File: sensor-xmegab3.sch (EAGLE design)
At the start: 59 parts, among them IC3 ATmega169PA, K1 SP6029TOP, M1 NRF24L01P-M, M2 DHT22, Q1 IRLML2502, Q2 IRLML2502, Q3 IRLML6402, U1 MCP1640C, U2 MCP604-I/ST

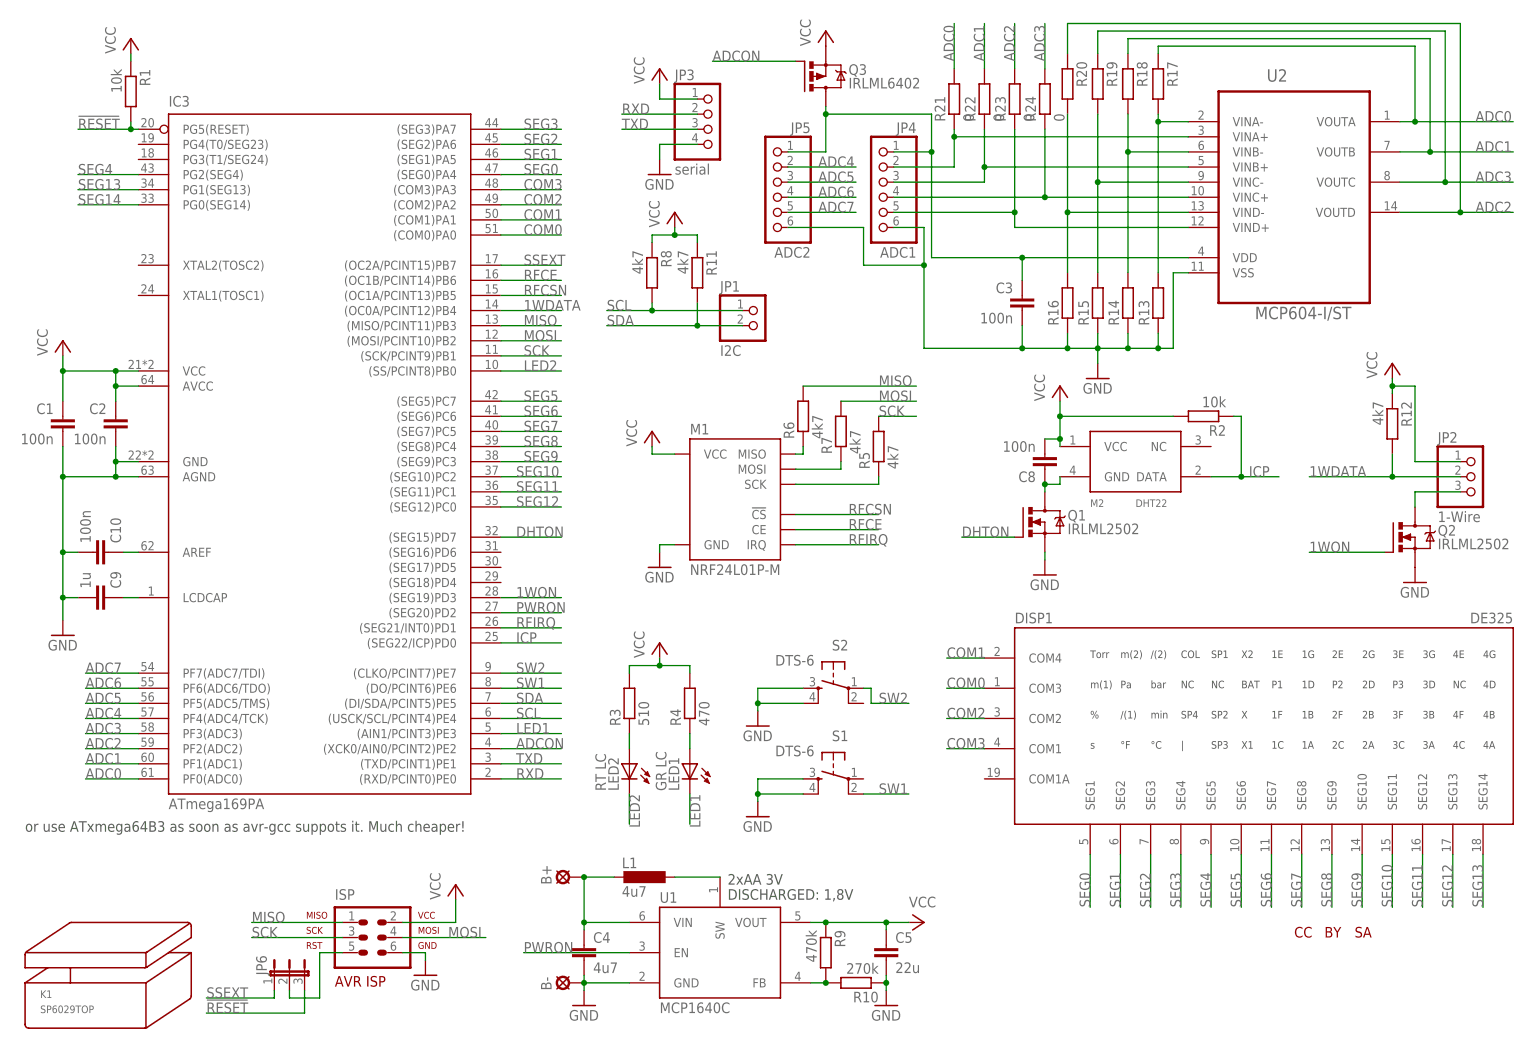
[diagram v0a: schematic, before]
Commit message: hanged to xmega, better performance at lower price
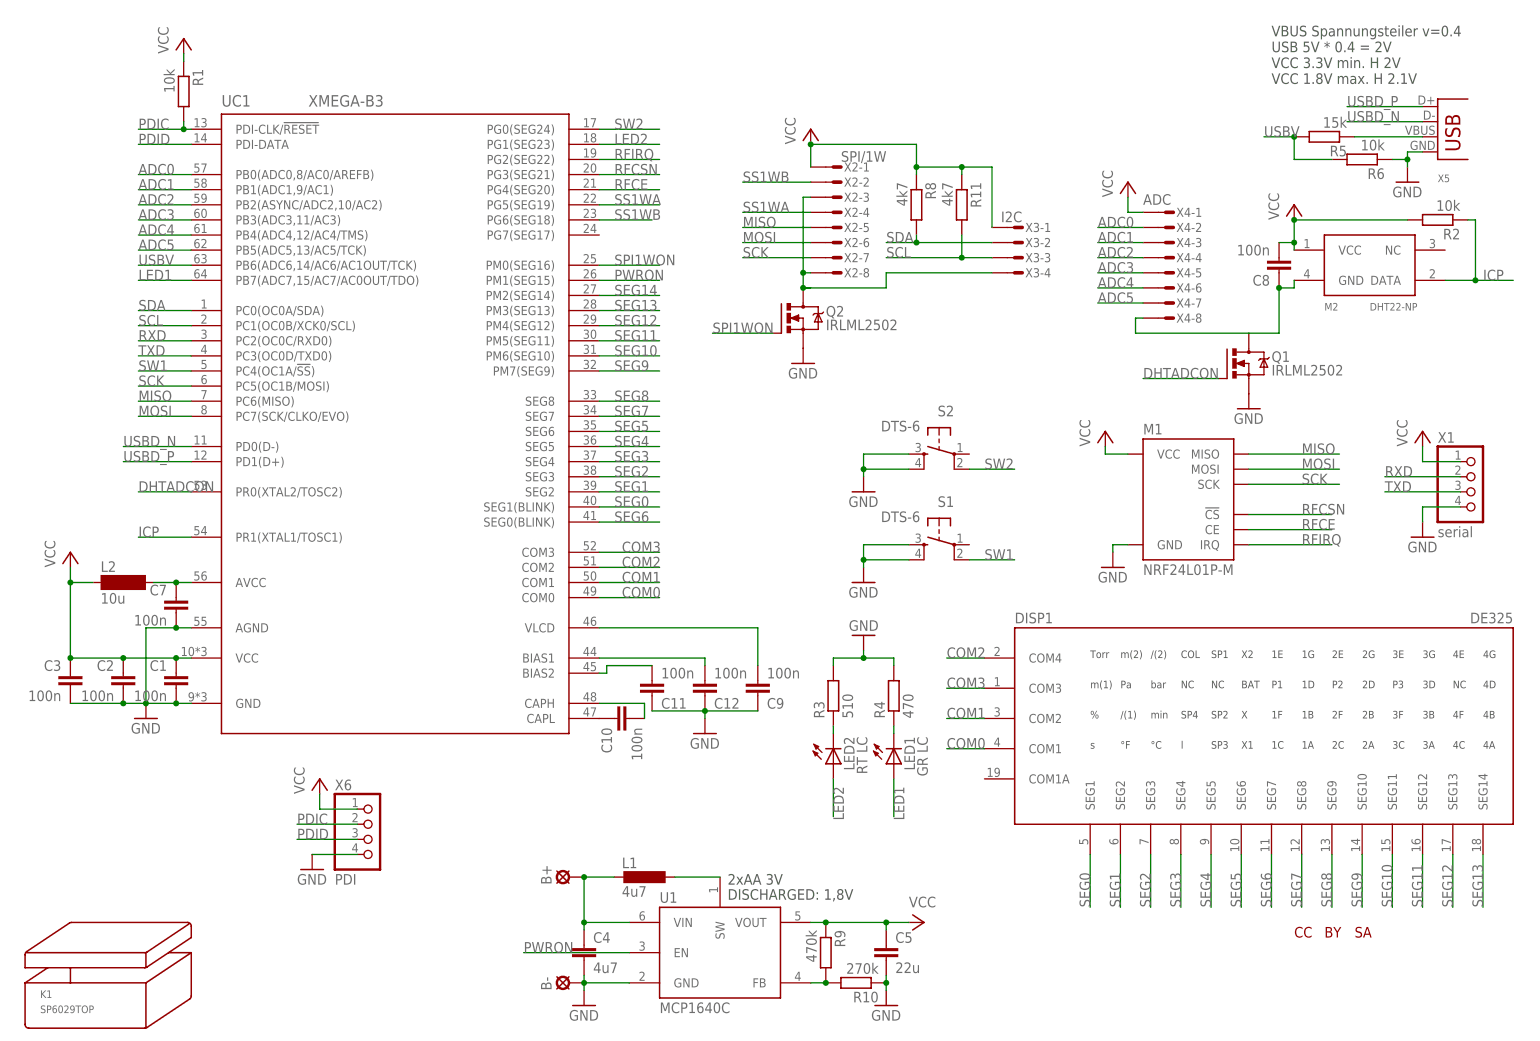
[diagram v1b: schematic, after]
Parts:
- removed IC3: ATmega169PA, avr-7:MEGA169-A
- removed ISP: ML6, avr-7:AVR-ISP-6VERT
- removed JP1: I2C, pinhead-mod:PINHD-1X2_2.54
- removed JP2: 1-Wire, pinhead-mod:PINHD-1X3_2.54
- removed JP3: serial, pinhead-mod:PINHD-1X4_2.54
- removed JP4: ADC1, pinhead-mod:PINHD-1X6_2.54
- removed JP5: ADC2, pinhead-mod:PINHD-1X6_2.54
- removed JP6: (no value), jumper:JP2E
- removed Q3: IRLML6402, mosfet:IRLML6402
- removed R12, R7: 4k7, rcl:R-EU_R0603
- removed R13, R14, R15, R16, R17, R18, R19, R20: (no value), rcl:R-EU_R0603
- removed R21, R22, R23, R24: 0, rcl:R-EU_R0201
- removed U2: MCP604-I/ST, microchip:MCP604-I/ST
- added C11, C12, C7: 100n, rcl:C-EUC0603
- added L2: 10u, inductor-neosid:SM-NE29
- added UC1: XMEGA-B3, avr-7:XMEGA-B3
- added X1: serial, pinhead-mod:PINHD-1X4_2.54
- added X2: SPI/1W, con-amp-micromatch:MICROMATCH-8
- added X3: I2C, con-amp-micromatch:MICROMATCH-4
- added X4: ADC, con-amp-micromatch:MICROMATCH-8
- added X5: (no value), con-usb:USB-MB-S
- added X6: PDI, pinhead-mod:PINHD-1X4_2.54
- C9: value 1u -> 100n
- M2: value DHT22 -> DHT22-NP; device modules:DHT22 -> modules:DHT22-NP
- R5: value 4k7 -> 15k
- R6: value 4k7 -> 10k
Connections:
- removed net !RESET: IC3.PG5(RESET), JP6.3, R1.2
- removed net 1WDATA: IC3.(OC0A/PCINT12)PB4, JP2.2, R12.2
- removed net 1WON: IC3.(SEG19)PD3, Q2.G
- removed net ADC6: IC3.PF6(ADC6/TDO), JP5.4
- removed net ADC7: IC3.PF7(ADC7/TDI), JP5.5
- removed net ADCON: IC3.(XCK0/AIN0/PCINT2)PE2, Q3.G
- removed net AREF: C10.1, IC3.AREF
- removed net DHTON: IC3.(SEG15)PD7, Q1.G
- removed net LCDCAP: C9.1, IC3.LCDCAP
- removed net N$13: LED1.A, R4.1
- removed net N$16: JP4.2, R21.1, U2.VINA+
- removed net N$17: C3.1, JP4.1, JP5.1, Q3.D, U2.VDD
- removed net N$18: R16.2, R20.2, U2.VIND-
- removed net N$19: R15.2, R19.2, U2.VINC-
- removed net N$2: C8.1, M2.GND, Q1.D
- removed net N$20: R14.2, R18.2, U2.VINB-
- removed net N$21: R13.2, R17.2, U2.VINA-
- removed net N$22: JP4.3, R22.1, U2.VINB+
- removed net N$24: JP4.5, R23.1, U2.VIND+
- removed net N$27: JP4.4, R24.1, U2.VINC+
- removed net N$4: M1.MOSI, R7.1
- removed net N$5: M1.SCK, R5.1
- removed net SSEXT: IC3.(OC2A/PCINT15)PB7, JP6.1
- new net AVCC: C7.1, L2.2, UC1.AVCC
- new net DHTADCON: Q1.G, UC1.PR0(XTAL2/TOSC2)
- new net N$10: C12.2, UC1.BIAS1
- new net N$12: C8.1, M2.GND, Q1.D, X4-8.S
- new net N$14: C9.2, UC1.VLCD
- new net N$23: C10.1, UC1.CAPL
- new net N$25: C10.2, UC1.CAPH
- new net N$9: C11.2, UC1.BIAS2
- new net PDIC: R1.2, UC1.PDI-CLK/!RESET, X6.2
- new net PDID: UC1.PDI-DATA, X6.3
- new net SPI1WON: Q2.G, UC1.PM0(SEG16)
- new net SS1WA: UC1.PG5(SEG19), X2-4.S
- new net SS1WB: UC1.PG6(SEG18), X2-2.S
- new net USBD_N: UC1.PD0(D-), X5.D-
- new net USBD_P: UC1.PD1(D+), X5.D+
- new net USBV: R5.2, R6.2, UC1.PB6(ADC6,14/AC6/AC1OUT/TCK)
- net ADC0: now also UC1.PB0(ADC0,8/AC0/AREFB), X4-2.S; no longer IC3.PF0(ADC0), R17.1, R21.2, U2.VOUTA
- net ADC1: now also UC1.PB1(ADC1,9/AC1), X4-3.S; no longer IC3.PF1(ADC1), R18.1, R22.2, U2.VOUTB
- net ADC2: now also UC1.PB2(ASYNC/ADC2,10/AC2), X4-4.S; no longer IC3.PF2(ADC2), R20.1, R23.2, U2.VOUTD
- net ADC3: now also UC1.PB3(ADC3,11/AC3), X4-5.S; no longer IC3.PF3(ADC3), R19.1, R24.2, U2.VOUTC
- net ADC4: now also UC1.PB4(ADC4,12/AC4/TMS), X4-6.S; no longer IC3.PF4(ADC4/TCK), JP5.2
- net ADC5: now also UC1.PB5(ADC5,13/AC5/TCK), X4-7.S; no longer IC3.PF5(ADC5/TMS), JP5.3
- net COM0: now also DISP1.COM1, UC1.COM0; no longer DISP1.COM3, IC3.(COM0)PA0
- net COM1: now also DISP1.COM2, UC1.COM1; no longer DISP1.COM4, IC3.(COM1)PA1
- net COM2: now also DISP1.COM4, UC1.COM2; no longer DISP1.COM2, IC3.(COM2)PA2
- net COM3: now also DISP1.COM3, UC1.COM3; no longer DISP1.COM1, IC3.(COM3)PA3
- net GND: now also C11.1, C12.1, C7.2, C9.1, R3.2, R4.2, R6.1, UC1.AGND, UC1.GND, X1.4, X5.GND, X6.4; no longer C10.2, C9.2, IC3.AGND, IC3.GND, ISP.6, JP3.4, JP4.6, JP5.6, R13.1, R14.1, R15.1, R16.1, U2.VSS
- net ICP: now also UC1.PR1(XTAL1/TOSC1); no longer IC3.(SEG22/ICP)PD0
- net LED1: now also LED1.A, UC1.PB7(ADC7,15/AC7/AC0OUT/TDO); no longer IC3.(AIN1/PCINT3)PE3, LED1.C
- net LED2: now also LED2.A, UC1.PG1(SEG23); no longer IC3.(SS/PCINT8)PB0, LED2.C
- net MISO: now also M1.MISO, UC1.PC6(MISO), X2-5.S; no longer IC3.(MISO/PCINT11)PB3, ISP.1, R6.2
- net MOSI: now also M1.MOSI, UC1.PC7(SCK/CLKO/EVO), X2-6.S; no longer IC3.(MOSI/PCINT10)PB2, ISP.4, R7.2
- net N$1: now also LED1.C, R4.1; no longer LED2.A, R3.1
- net N$11: now also X2-3.S, X2-8.S, X3-4.S; no longer JP2.3
- net N$3: now also R5.1, X5.VBUS; no longer M1.MISO, R6.1
- net N$6: now also LED2.C, R3.1; no longer ISP.5, JP6.2
- net PWRON: now also UC1.PM1(SEG15); no longer IC3.(SEG20)PD2
- net RFCE: now also UC1.PG4(SEG20); no longer IC3.(OC1B/PCINT14)PB6
- net RFCSN: now also UC1.PG3(SEG21); no longer IC3.(OC1A/PCINT13)PB5
- net RFIRQ: now also UC1.PG2(SEG22); no longer IC3.(SEG21/INT0)PD1
- net RXD: now also UC1.PC2(OC0C/RXD0), X1.2; no longer IC3.(RXD/PCINT0)PE0, JP3.2
- net SCK: now also M1.SCK, UC1.PC5(OC1B/MOSI), X2-7.S; no longer IC3.(SCK/PCINT9)PB1, ISP.3, R5.2
- net SCL: now also R11.2, UC1.PC1(OC0B/XCK0/SCL), X3-3.S; no longer IC3.(USCK/SCL/PCINT4)PE4, JP1.1, R8.2
- net SDA: now also R8.2, UC1.PC0(OC0A/SDA), X3-2.S; no longer IC3.(DI/SDA/PCINT5)PE5, JP1.2, R11.2
- net SEG0: now also UC1.SEG1(BLINK); no longer IC3.(SEG0)PA4
- net SEG1: now also UC1.SEG2; no longer IC3.(SEG1)PA5
- net SEG10: now also UC1.PM6(SEG10); no longer IC3.(SEG10)PC2
- net SEG11: now also UC1.PM5(SEG11); no longer IC3.(SEG11)PC1
- net SEG12: now also UC1.PM4(SEG12); no longer IC3.(SEG12)PC0
- net SEG13: now also UC1.PM3(SEG13); no longer IC3.PG1(SEG13)
- net SEG14: now also UC1.PM2(SEG14); no longer IC3.PG0(SEG14)
- net SEG2: now also UC1.SEG3; no longer IC3.(SEG2)PA6
- net SEG3: now also UC1.SEG4; no longer IC3.(SEG3)PA7
- net SEG4: now also UC1.SEG5; no longer IC3.PG2(SEG4)
- net SEG5: now also UC1.SEG6; no longer IC3.(SEG5)PC7
- net SEG6: now also UC1.SEG0(BLINK); no longer IC3.(SEG6)PC6
- net SEG7: now also UC1.SEG7; no longer IC3.(SEG7)PC5
- net SEG8: now also UC1.SEG8; no longer IC3.(SEG8)PC4
- net SEG9: now also UC1.PM7(SEG9); no longer IC3.(SEG9)PC3
- net SW1: now also UC1.PC4(OC1A/!SS!); no longer IC3.(DO/PCINT6)PE6
- net SW2: now also S2.2, UC1.PG0(SEG24); no longer IC3.(CLKO/PCINT7)PE7, S2.1
- net TXD: now also UC1.PC3(OC0D/TXD0), X1.3; no longer IC3.(TXD/PCINT1)PE1, JP3.3
- net VCC: now also C3.1, L2.1, UC1.VCC, X1.1, X2-1.S, X3-1.S, X4-1.S, X6.1; no longer IC3.AVCC, IC3.VCC, ISP.2, JP2.1, JP3.1, Q3.S, R12.1, R3.2, R4.2
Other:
- note added: "VBUS Spannungsteiler v=0.4 USB 5V * 0.4 = 2V VCC 3.3V min. H 2V VCC 1.8V max. H 2.1V"
- note removed: "or use ATxmega64B3 as soon as avr-gcc suppots it. Much cheaper!"
- moved on the sheet: C1, C10, C2, C3, C8, C9, LED1, LED2, M1, M2, Q1, Q2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

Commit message: some rerouting
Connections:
- removed net SEG14: UC1.PM2(SEG14)
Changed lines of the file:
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@@
 <grid distance="1.27" unitdist="mm" unit="mm" style="lines" multiple="1" display="yes" altdistance="635" altunitdist="mic" altunit="mic"/>
 <layers>
-<layer number="1" name="Top" color="4" fill="1" visible="yes" active="no"/>
-<layer number="2" name="Route2" color="1" fill="3" visible="yes" active="no"/>
-<layer number="3" name="Route3" color="4" fill="3" visible="yes" active="no"/>
-<layer number="4" name="Route4" color="1" fill="4" visible="yes" active="no"/>
-<layer number="5" name="Route5" color="4" fill="4" visible="yes" active="no"/>
-<layer number="6" name="Route6" color="1" fill="8" visible="yes" active="no"/>
-<layer number="7" name="Route7" color="4" fill="8" visible="yes" active="no"/>
-<layer number="8" name="Route8" color="1" fill="2" visible="yes" active="no"/>
-<layer number="9" name="Route9" color="4" fill="2" visible="yes" active="no"/>
-<layer number="10" name="Route10" color="1" fill="7" visible="yes" active="no"/>
-<layer number="11" name="Route11" color="4" fill="7" visible="yes" active="no"/>
-<layer number="12" name="Route12" color="1" fill="5" visible="yes" active="no"/>
-<layer number="13" name="Route13" color="4" fill="5" visible="yes" active="no"/>
-<layer number="14" name="Route14" color="1" fill="6" visible="yes" active="no"/>
-<layer number="15" name="Route15" color="4" fill="6" visible="yes" active="no"/>
-<layer number="16" name="Bottom" color="1" fill="1" visible="yes" active="no"/>
-<layer number="17" name="Pads" color="2" fill="1" visible="yes" active="no"/>
-<layer number="18" name="Vias" color="2" fill="1" visible="yes" active="no"/>
-<layer number="19" name="Unrouted" color="6" fill="1" visible="yes" active="no"/>
-<layer number="20" name="Dimension" color="15" fill="1" visible="yes" active="no"/>
-<layer number="21" name="tPlace" color="7" fill="1" visible="yes" active="no"/>
-<layer number="22" name="bPlace" color="7" fill="1" visible="yes" active="no"/>
-<layer number="23" name="tOrigins" color="15" fill="1" visible="yes" active="no"/>
-<layer number="24" name="bOrigins" color="15" fill="1" visible="yes" active="no"/>
-<layer number="25" name="tNames" color="7" fill="1" visible="yes" active="no"/>
-<layer number="26" name="bNames" color="7" fill="1" visible="yes" active="no"/>
-<layer number="27" name="tValues" color="7" fill="1" visible="yes" active="no"/>
-<layer number="28" name="bValues" color="7" fill="1" visible="yes" active="no"/>
+<layer number="1" name="Top" color="4" fill="1" visible="no" active="no"/>
+<layer number="2" name="Route2" color="1" fill="3" visible="no" active="no"/>
+<layer number="3" name="Route3" color="4" fill="3" visible="no" active="no"/>
+<layer number="4" name="Route4" color="1" fill="4" visible="no" active="no"/>
+<layer number="5" name="Route5" color="4" fill="4" visible="no" active="no"/>
+<layer number="6" name="Route6" color="1" fill="8" visible="no" active="no"/>
+<layer number="7" name="Route7" color="4" fill="8" visible="no" active="no"/>
+<layer number="8" name="Route8" color="1" fill="2" visible="no" active="no"/>
+<layer number="9" name="Route9" color="4" fill="2" visible="no" active="no"/>
+<layer number="10" name="Route10" color="1" fill="7" visible="no" active="no"/>
+<layer number="11" name="Route11" color="4" fill="7" visible="no" active="no"/>
+<layer number="12" name="Route12" color="1" fill="5" visible="no" active="no"/>
+<layer number="13" name="Route13" color="4" fill="5" visible="no" active="no"/>
+<layer number="14" name="Route14" color="1" fill="6" visible="no" active="no"/>
+<layer number="15" name="Route15" color="4" fill="6" visible="no" active="no"/>
+<layer number="16" name="Bottom" color="1" fill="1" visible="no" active="no"/>
+<layer number="17" name="Pads" color="2" fill="1" visible="no" active="no"/>
+<layer number="18" name="Vias" color="2" fill="1" visible="no" active="no"/>
+<layer number="19" name="Unrouted" color="6" fill="1" visible="no" active="no"/>
+<layer number="20" name="Dimension" color="15" fill="1" visible="no" active="no"/>
+<layer number="21" name="tPlace" color="7" fill="1" visible="no" active="no"/>
+<layer number="22" name="bPlace" color="7" fill="1" visible="no" active="no"/>
+<layer number="23" name="tOrigins" color="15" fill="1" visible="no" active="no"/>
+<layer number="24" name="bOrigins" color="15" fill="1" visible="no" active="no"/>
+<layer number="25" name="tNames" color="7" fill="1" visible="no" active="no"/>
+<layer number="26" name="bNames" color="7" fill="1" visible="no" active="no"/>
+<layer number="27" name="tValues" color="7" fill="1" visible="no" active="no"/>
+<layer number="28" name="bValues" color="7" fill="1" visible="no" active="no"/>
 <layer number="29" name="tStop" color="7" fill="3" visible="no" active="no"/>
 <layer number="30" name="bStop" color="7" fill="6" visible="no" active="no"/>
@@
 <layer number="35" name="tGlue" color="7" fill="4" visible="no" active="no"/>
 <layer number="36" name="bGlue" color="7" fill="5" visible="no" active="no"/>
-<layer number="37" name="tTest" color="7" fill="1" visible="yes" active="no"/>
-<layer number="38" name="bTest" color="7" fill="1" visible="yes" active="no"/>
+<layer number="37" name="tTest" color="7" fill="1" visible="no" active="no"/>
+<layer number="38" name="bTest" color="7" fill="1" visible="no" active="no"/>
 <layer number="39" name="tKeepout" color="4" fill="11" visible="no" active="no"/>
 <layer number="40" name="bKeepout" color="1" fill="11" visible="no" active="no"/>
@@
 <layer number="44" name="Drills" color="7" fill="1" visible="no" active="no"/>
 <layer number="45" name="Holes" color="7" fill="1" visible="no" active="no"/>
-<layer number="46" name="Milling" color="3" fill="1" visible="yes" active="no"/>
-<layer number="47" name="Measures" color="7" fill="1" visible="yes" active="no"/>
-<layer number="48" name="Document" color="7" fill="1" visible="yes" active="no"/>
-<layer number="49" name="Reference" color="7" fill="1" visible="yes" active="no"/>
-<layer number="50" name="dxf" color="7" fill="1" visible="yes" active="no"/>
-<layer number="51" name="tDocu" color="7" fill="1" visible="yes" active="no"/>
-<layer number="52" name="bDocu" color="7" fill="1" visible="yes" active="no"/>
-<layer number="53" name="tGND_GNDA" color="7" fill="9" visible="yes" active="no"/>
-<layer number="54" name="bGND_GNDA" color="1" fill="9" visible="yes" active="no"/>
-<layer number="56" name="wert" color="7" fill="1" visible="yes" active="no"/>
+<layer number="46" name="Milling" color="3" fill="1" visible="no" active="no"/>
+<layer number="47" name="Measures" color="7" fill="1" visible="no" active="no"/>
+<layer number="48" name="Document" color="7" fill="1" visible="no" active="no"/>
+<layer number="49" name="Reference" color="7" fill="1" visible="no" active="no"/>
+<layer number="50" name="dxf" color="7" fill="1" visible="no" active="no"/>
+<layer number="51" name="tDocu" color="7" fill="1" visible="no" active="no"/>
+<layer number="52" name="bDocu" color="7" fill="1" visible="no" active="no"/>
+<layer number="53" name="tGND_GNDA" color="7" fill="9" visible="no" active="no"/>
+<layer number="54" name="bGND_GNDA" color="1" fill="9" visible="no" active="no"/>
+<layer number="56" name="wert" color="7" fill="1" visible="no" active="no"/>
 <layer number="91" name="Nets" color="2" fill="1" visible="yes" active="yes"/>
 <layer number="92" name="Busses" color="1" fill="1" visible="yes" active="yes"/>
@@
 </segment>
 </net>
-<net name="SEG14" class="0">
-<segment>
-<wire x1="101.6" y1="128.27" x2="111.76" y2="128.27" width="0.1524" layer="91"/>
-<label x="104.14" y="128.27" size="1.778" layer="95"/>
-<pinref part="UC1" gate="G$1" pin="PM2(SEG14)"/>
-</segment>
-</net>
 <net name="MISO" class="0">
 <segment>
@@
 <pinref part="X4" gate="-8" pin="S"/>
 <wire x1="191.77" y1="124.46" x2="193.04" y2="124.46" width="0.1524" layer="91"/>
-</segment>
-</net>
+<junction x="210.82" y="121.92"/>
+</segment>
+</net>
